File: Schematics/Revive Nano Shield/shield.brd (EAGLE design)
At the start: 43.5 x 69.2 mm, 24 parts

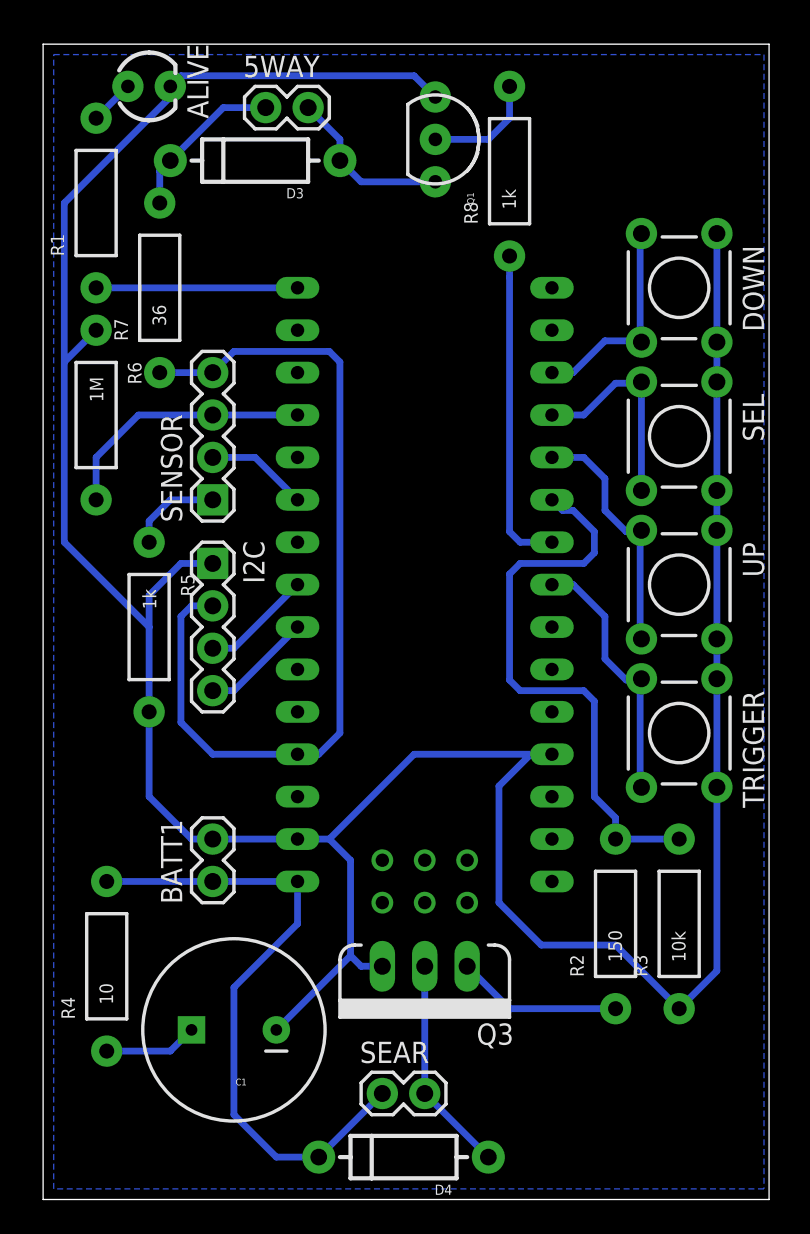
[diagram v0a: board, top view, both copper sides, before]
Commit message: Updates nano design to be more compact
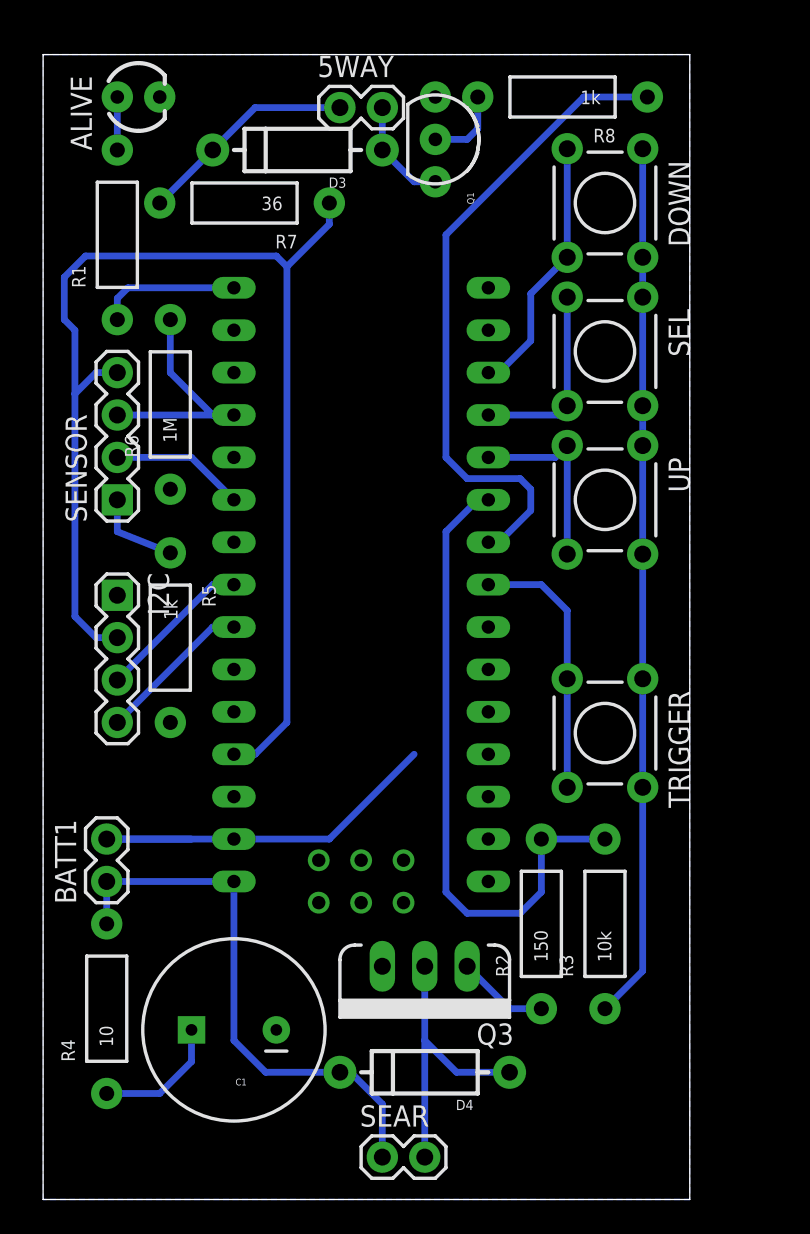
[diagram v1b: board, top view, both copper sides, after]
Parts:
- moved R7 7.18 mm to (12.1, 59.7), turned to 180 degrees
- moved DOWN 6.75 mm to (33.7, 59.7)
- moved SEL 6.75 mm to (33.7, 50.8)
- moved UP 6.75 mm to (33.7, 41.9)
- moved BATT1 6.35 mm to (3.81, 19.1)
- moved I2C 6.02 mm to (4.45, 36.2)
- moved SENSOR 5.71 mm to (4.45, 41.9)
- moved R8 5.46 mm to (31.1, 66.0), turned to 180 degrees
- moved D4 5.24 mm to (22.9, 7.62)
- moved R6 4.49 mm to (7.62, 47.6), turned to 90 degrees
- moved 5WAY 4.45 mm to (17.8, 65.4)
- moved R2 4.45 mm to (29.8, 16.5)
- moved R3 4.45 mm to (33.7, 16.5)
- moved TRIGGER 4.45 mm to (33.7, 27.9)
- moved SEAR 3.81 mm to (20.3, 2.54)
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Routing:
- net GND: track 188.1 -> 78.7 mm
- net 5V: track 53.2 -> 77.0 mm
- net 5WAY: track 19.3 -> 39.3 mm
- net 9V: track 38.5 -> 33.3 mm
- net N$3: track 9.94 -> 5.50 mm
- net N$7: track 13.0 -> 17.3 mm
- net SEAR: track 34.8 -> 38.7 mm
- net N$15: track 10.2 -> 6.50 mm
- net KEEP_ALIVE: track 12.1 -> 8.52 mm
- net N$5: track 9.83 -> 13.2 mm
- net UP_BTN: track 14.8 -> 11.5 mm
- net DWN_BTN: track 12.6 -> 15.7 mm
- net SDA: track 6.66 -> 9.35 mm
- net SCL: track 6.66 -> 9.35 mm
- net N$4: track 5.61 -> 7.77 mm
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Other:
- board size 43.5 x 69.2 mm -> 38.7 x 68.6 mm

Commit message: Updates nano design so USB port is accessible while connected
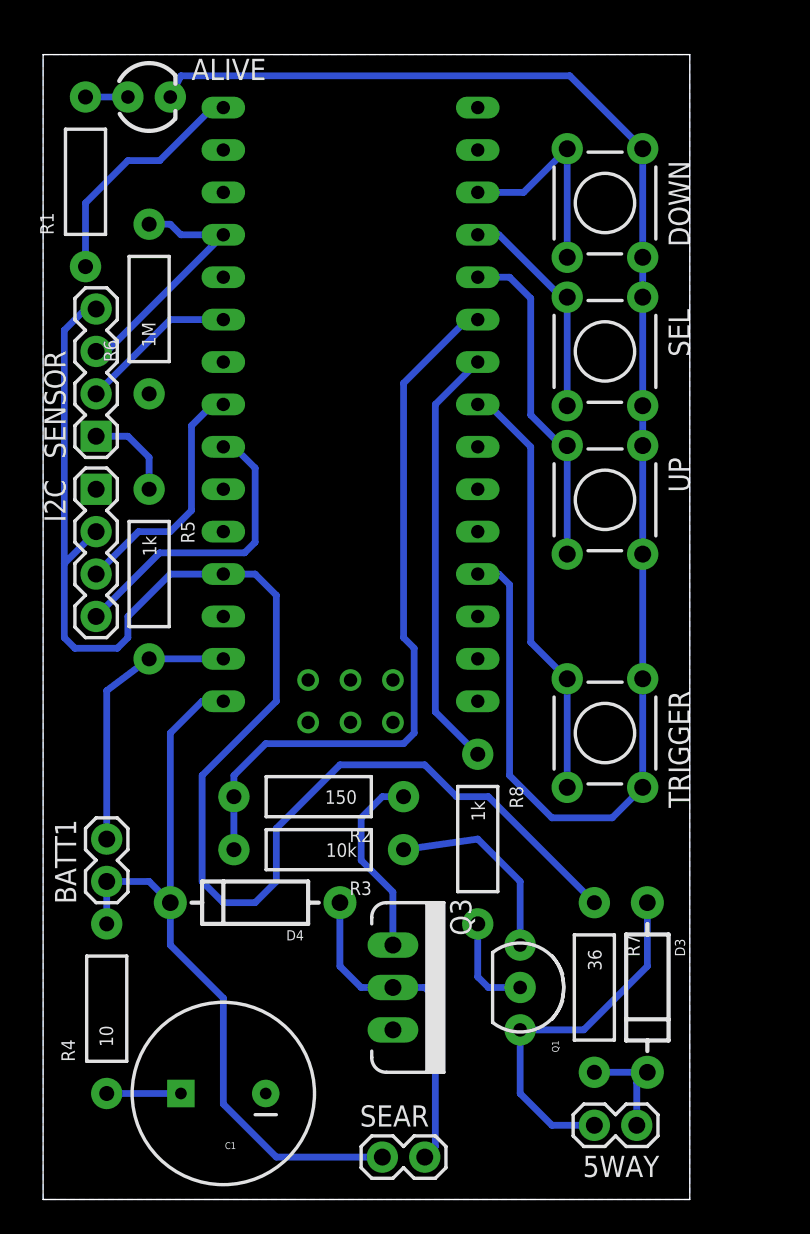
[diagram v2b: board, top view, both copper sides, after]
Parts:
- moved 5WAY 63.5 mm to (35.6, 4.45), turned to 180 degrees
- moved D3 54.4 mm to (36.2, 12.7), turned to 270 degrees
- moved R7 51.5 mm to (33.0, 12.7), turned to 270 degrees
- moved Q1 51.1 mm to (28.6, 12.7)
- moved R8 44.7 mm to (26.0, 21.6), turned to 270 degrees
- moved R3 17.7 mm to (16.5, 21.0), turned to 180 degrees
- moved R2 15.4 mm to (16.5, 24.1), turned to 180 degrees
- moved D4 14.4 mm to (12.7, 17.8)
- moved U$5 10.8 mm to (21.0, 38.7)
- moved I2C 6.48 mm to (3.17, 42.5)
- moved R6 5.85 mm to (6.35, 53.3)
- moved R5 4.02 mm to (6.35, 37.5)
- moved SENSOR 4.02 mm to (3.17, 45.7)
- moved C1 3.86 mm to (10.8, 6.35)
- moved R1 3.70 mm to (2.54, 61.0)
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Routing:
- net GND: track 78.7 -> 120.9 mm
- net N$15: track 6.50 -> 22.1 mm
- net 5V: track 77.0 -> 91.3 mm
- net 5WAY: track 39.3 -> 25.6 mm
- net 9V: track 33.3 -> 45.2 mm
- net TRIGGER: track 16.0 -> 25.5 mm
- net SCL: track 9.35 -> 18.2 mm
- net UP_BTN: track 11.5 -> 20.1 mm
- net N$5: track 13.2 -> 6.61 mm
- net N$3: track 5.50 -> 11.5 mm
- net KEEP_ALIVE: track 8.52 -> 14.4 mm
- net SDA: track 9.35 -> 14.8 mm
- net SEAR: track 38.7 -> 43.5 mm
- net N$4: track 7.77 -> 4.45 mm
- net N$7: track 17.3 -> 20.1 mm
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
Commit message: Reworks pins to match with new Nano board design
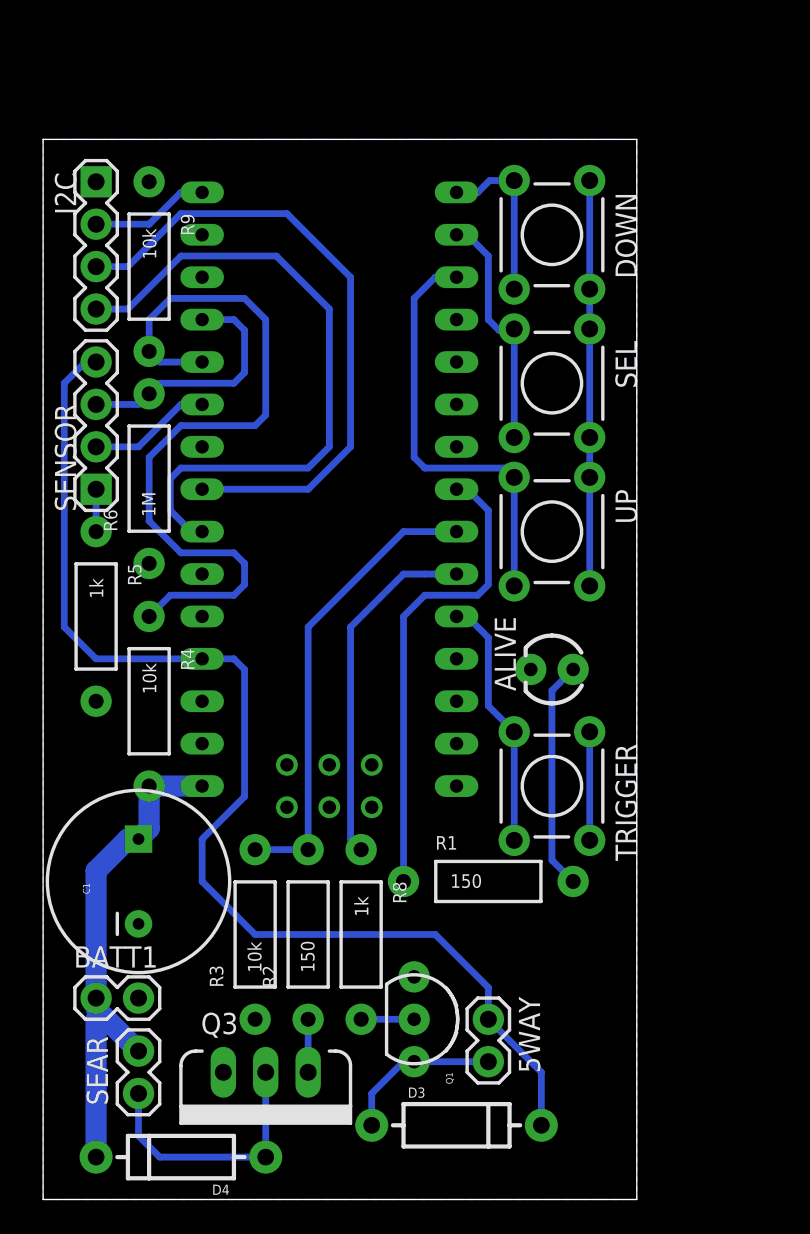
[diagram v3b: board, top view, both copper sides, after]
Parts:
- removed R7: 36, SparkFun:AXIAL-0.4
- added R9: 10k, SparkFun:AXIAL-0.4
- R1: value (none) -> 150
- R4: value 10 -> 10k
- moved R1 48.4 mm to (26.7, 19.1), turned to 0 degrees
- moved ALIVE 41.9 mm to (30.5, 31.8), turned to 180 degrees
- moved R4 18.6 mm to (6.35, 29.8), turned to 270 degrees
- moved I2C 18.4 mm to (3.17, 61.0)
- moved SEAR 15.9 mm to (5.71, 8.89), turned to 270 degrees
- moved D4 15.9 mm to (8.26, 2.54)
- moved D3 14.1 mm to (24.8, 4.45), turned to 0 degrees
- moved C1 13.7 mm to (5.71, 19.1), turned to 90 degrees
- moved 5WAY 10.9 mm to (26.7, 10.8), turned to 270 degrees
- moved R6 10.2 mm to (6.35, 43.2)
- moved Q3 9.16 mm to (13.3, 7.62), turned to 180 degrees
- moved R8 9.03 mm to (19.1, 15.9)
- moved R2 8.28 mm to (15.9, 15.9), turned to 90 degrees
- moved BATT1 7.01 mm to (3.17, 12.1), turned to 0 degrees
- moved Q1 6.63 mm to (22.2, 10.8)
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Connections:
- removed net N$4: C1.1, R4.P$1
- removed net N$5: 5WAY.1, D3.C, R7.P$2
- new net BATT_STATUS: R4.P$1, R9.P$2, U$5.A1
- new net OLED_PWR: I2C.2, U$5.D13
- net 5V: now also 5WAY.1, D3.C; no longer I2C.2, R7.P$1
- net 5WAY: now also U$5.D3; no longer U$5.D6
- net 9V: now also C1.1
- net DWN_BTN: now also U$5.D12; no longer U$5.D10
- net GND: now also R9.P$1
- net KEEP_ALIVE: now also U$5.D5; no longer U$5.D13
- net SEAR: now also U$5.D4; no longer U$5.D7
- net SEL_BTN: now also U$5.D11; no longer U$5.D9
- net TRIGGER: now also U$5.D2; no longer U$5.D5
- net UP_BTN: now also U$5.D10; no longer U$5.D8
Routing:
- net GND: track 120.9 -> 30.8 mm
- net BATT_STATUS: track 0.00 -> 45.5 mm
- net SDA: track 14.8 -> 38.2 mm
- net SCL: track 18.2 -> 39.5 mm
- net 5V: track 91.3 -> 72.0 mm
- net SEAR: track 43.5 -> 27.8 mm
- net KEEP_ALIVE: track 14.4 -> 28.6 mm
- net 9V: track 45.2 -> 31.3 mm
- net N$15: track 22.1 -> 9.68 mm
- net N$2: track 2.54 -> 13.8 mm
- net TRIGGER: track 25.5 -> 15.2 mm
- net N$3: track 11.5 -> 3.17 mm
- net OLED_PWR: track 0.00 -> 7.77 mm
- net N$5: track 6.61 -> 0.00 mm
- net UP_BTN: track 20.1 -> 25.6 mm
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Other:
- board size 38.7 x 68.6 mm -> 35.6 x 63.5 mm
